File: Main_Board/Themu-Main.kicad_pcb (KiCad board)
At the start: 2 copper layers, 20.1 x 56.6 mm, 49 parts, among them J1 USB_B_Micro, J2 Conn_01x02, J3 Conn_01x08, Q1 mmbt2222, Q2 mmbt2222, Q3 DMP2045U, U1 CP2104, U2 AP2112K-3.3, U3 ESP32-WROOM-32, U4 MCP73831-2-OT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

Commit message: Added adapter board for 5 flex sensors and 1 button
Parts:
- L1: footprint Themu_FP_Lib:LED APTF1616LSEEZGKQBKC -> Main_Board:LED_APTF1616LSEEZGKQBKC
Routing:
- net GND: vias 17 -> 12
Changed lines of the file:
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@@
     (thickness 1.6)
     (drawings 4)
-    (tracks 898)
+    (tracks 894)
     (zones 0)
     (modules 49)
@@
     (add_net VBUS)
   )
+  (module Main_Board:LED_APTF1616LSEEZGKQBKC (layer F.Cu)
+    (at 111.506 75.946 270)
+    (fp_text reference L1 (at 0 2.032 90) (layer F.SilkS)
+      (effects (font (size 1 1) (thickness 0.15)))
+    )
+    (fp_text value LED_ARGB (at 0 -1.905 90) (layer F.Fab)
+      (effects (font (size 1 1) (thickness 0.15)))
+    )
+    (fp_line (start -0.127 -0.8) (end 0.127 -0.8) (layer F.SilkS) (width 0.12))
+    (fp_line (start -0.127 0.8) (end 0.127 0.8) (layer F.SilkS) (width 0.12))
+    (fp_line (start -1.524 -1.016) (end 1.524 -1.016) (layer F.CrtYd) (width 0.05))
+    (fp_line (start 1.524 -1.016) (end 1.524 1.016) (layer F.CrtYd) (width 0.05))
+    (fp_line (start 1.524 1.016) (end -1.524 1.016) (layer F.CrtYd) (width 0.05))
+    (fp_line (start -1.524 1.016) (end -1.524 -1.016) (layer F.CrtYd) (width 0.05))
+    (fp_line (start 0.127 0.254) (end 0.127 0.8) (layer F.SilkS) (width 0.12))
+    (pad 4 smd rect (at 0.875 -0.5 270) (size 0.85 0.5) (layers F.Cu F.Paste F.Mask)
+      (net 37 "Net-(L1-Pad4)"))
+    (pad 1 smd rect (at 0.875 0.5 270) (size 0.85 0.5) (layers F.Cu F.Paste F.Mask)
+      (net 2 +3V3))
+    (pad 2 smd rect (at -0.875 0.5 270) (size 0.85 0.5) (layers F.Cu F.Paste F.Mask)
+      (net 32 "Net-(L1-Pad2)"))
+    (pad 3 smd rect (at -0.875 -0.5 270) (size 0.85 0.5) (layers F.Cu F.Paste F.Mask)
+      (net 31 "Net-(L1-Pad3)"))
+    (model "C:/Users/germi/Downloads/User Library-LED_0605/User Library-LED_0605.STEP"
+      (at (xyz 0 0 0))
+      (scale (xyz 1 1 1))
+      (rotate (xyz 0 0 0))
+    )
+  )
   (module RF_Module:ESP32-WROOM-32 (layer F.Cu)
     (at 103.124 56.007)
@@
     )
   )
-  (module "Themu_FP_Lib:LED APTF1616LSEEZGKQBKC" (layer F.Cu)
-    (at 111.506 75.946 270)
-    (fp_text reference L1 (at -2.286 -0.635 90) (layer F.SilkS)
-      (effects (font (size 0.7 0.7) (thickness 0.1524)))
-    )
-    (fp_text value LED_ARGB (at 0 -1.905 90) (layer F.Fab)
-      (effects (font (size 1 1) (thickness 0.15)))
-    )
-    (fp_line (start -0.127 -0.8) (end 0.127 -0.8) (layer F.SilkS) (width 0.12))
-    (fp_line (start -0.127 0.8) (end 0.127 0.8) (layer F.SilkS) (width 0.12))
-    (fp_line (start -1.524 -1.016) (end 1.524 -1.016) (layer F.CrtYd) (width 0.05))
-    (fp_line (start 1.524 -1.016) (end 1.524 1.016) (layer F.CrtYd) (width 0.05))
-    (fp_line (start 1.524 1.016) (end -1.524 1.016) (layer F.CrtYd) (width 0.05))
-    (fp_line (start -1.524 1.016) (end -1.524 -1.016) (layer F.CrtYd) (width 0.05))
-    (fp_line (start 0.127 0.254) (end 0.127 0.8) (layer F.SilkS) (width 0.12))
-    (pad 4 smd rect (at 0.875 -0.5 270) (size 0.85 0.5) (layers F.Cu F.Paste F.Mask)
-      (net 37 "Net-(L1-Pad4)"))
-    (pad 1 smd rect (at 0.875 0.5 270) (size 0.85 0.5) (layers F.Cu F.Paste F.Mask)
-      (net 2 +3V3))
-    (pad 2 smd rect (at -0.875 0.5 270) (size 0.85 0.5) (layers F.Cu F.Paste F.Mask)
-      (net 32 "Net-(L1-Pad2)"))
-    (pad 3 smd rect (at -0.875 -0.5 270) (size 0.85 0.5) (layers F.Cu F.Paste F.Mask)
-      (net 31 "Net-(L1-Pad3)"))
-    (model "C:/Users/germi/Downloads/User Library-LED_0605/User Library-LED_0605.STEP"
-      (at (xyz 0 0 0))
-      (scale (xyz 1 1 1))
-      (rotate (xyz 0 0 0))
-    )
-  )
   (module Connector_JST:JST_PH_S2B-PH-K_1x02_P2.00mm_Horizontal (layer F.Cu)
     (at 101.727 91.694 270)
@@
     (tags "capacitor handsolder")
     (attr smd)
-    (fp_text reference C10 (at 0.127 -4.826 90) (layer B.SilkS)
+    (fp_text reference C10 (at -0.889 -8.001 90) (layer B.SilkS)
       (effects (font (size 0.7 0.7) (thickness 0.1524)) (justify mirror))
     )
@@
     (tags "capacitor handsolder")
     (attr smd)
-    (fp_text reference C11 (at 0.127 -5.334 90) (layer B.SilkS)
+    (fp_text reference C11 (at -0.127 -8.382 90) (layer B.SilkS)
       (effects (font (size 0.7 0.7) (thickness 0.1524)) (justify mirror))
     )
@@
     (tags "resistor handsolder")
     (attr smd)
-    (fp_text reference R13 (at 0.127 -4.318 90) (layer B.SilkS)
+    (fp_text reference R13 (at -1.778 -7.493 90) (layer B.SilkS)
       (effects (font (size 0.7 0.7) (thickness 0.1524)) (justify mirror))
     )
@@
   (gr_line (start 113.157 96.393) (end 93.091 96.393) (layer Edge.Cuts) (width 0.1))
   (via (at 100.457 56.896) (size 0.8) (drill 0.4) (layers F.Cu B.Cu) (net 1))
-  (via (at 102.235 53.213) (size 0.8) (drill 0.4) (layers F.Cu B.Cu) (net 1))
-  (via (at 102.997 56.134) (size 0.8) (drill 0.4) (layers F.Cu B.Cu) (net 1))
-  (via (at 101.346 56.134) (size 0.8) (drill 0.4) (layers F.Cu B.Cu) (net 1))
-  (via (at 103.759 56.896) (size 0.8) (drill 0.4) (layers F.Cu B.Cu) (net 1))
   (via (at 107.315 71.882) (size 0.8) (drill 0.4) (layers F.Cu B.Cu) (net 1))
   (segment (start 109.728 75.071) (end 109.728 74.168) (width 0.1524) (layer F.Cu) (net 1))
@@
   (segment (start 94.615 46.609) (end 111.633 46.609) (width 0.1524) (layer F.Cu) (net 1))
   (segment (start 102.124 56.88) (end 102.124 55.252) (width 0.1524) (layer F.Cu) (net 1))
-  (via (at 102.124 56.88) (size 0.8) (drill 0.4) (layers F.Cu B.Cu) (net 1))
   (segment (start 109.855 49.911) (end 108.712 51.054) (width 0.1524) (layer B.Cu) (net 1))
   (segment (start 102.124 55.252) (end 102.124 55.252) (width 0.1524) (layer F.Cu) (net 1))
   (segment (start 102.183 55.193) (end 102.124 55.252) (width 0.1524) (layer F.Cu) (net 1))
-  (via (at 102.183 55.193) (size 0.8) (drill 0.4) (layers F.Cu B.Cu) (net 1))
   (segment (start 109.22 79.756) (end 109.728 79.248) (width 0.1524) (layer F.Cu) (net 1))
   (segment (start 109.728 79.248) (end 110.998 79.248) (width 0.1524) (layer F.Cu) (net 1))
@@
   (segment (start 102.235 60.452) (end 102.235 59.055) (width 0.1524) (layer F.Cu) (net 1))
   (segment (start 102.235 59.055) (end 102.124 58.944) (width 0.1524) (layer F.Cu) (net 1))
+  (segment (start 102.124 55.252) (end 102.124 55.252) (width 0.1524) (layer F.Cu) (net 1))
+  (via (at 102.124 55.252) (size 3) (drill 2.8) (layers F.Cu B.Cu) (net 1) (status 1000000))
   (segment (start 101.854 78.867) (end 101.8215 78.8345) (width 0.1524) (layer F.Cu) (net 2))
   (segment (start 108.27 80.434) (end 108.27 78.801) (width 0.1524) (layer F.Cu) (net 2))
@@
     (connect_pads (clearance 0.3048))
     (min_thickness 0.1524)
-    (fill yes (arc_segments 32) (thermal_gap 0.254) (thermal_bridge_width 0.2032))
+    (fill yes (arc_segments 32) (thermal_gap 0.254) (thermal_bridge_width 0.3))
     (polygon
       (pts
@@
     (connect_pads (clearance 0.3048))
     (min_thickness 0.1524)
-    (fill yes (arc_segments 32) (thermal_gap 0.254) (thermal_bridge_width 0.2032))
+    (fill yes (arc_segments 32) (thermal_gap 0.254) (thermal_bridge_width 0.3))
     (polygon
       (pts

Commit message: Partial commit
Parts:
- added R22: 1K, Resistor_SMD:R_0603_1608Metric_Pad1.05x0.95mm_HandSolder, F.Cu at (118.4, 77.7)
- R15, R16, R17, R18, R19: value 1K -> 47K
- moved J3 51.6 mm to (132.6, 52.3), turned to 90 degrees
- moved R11 35.7 mm to (132.0, 58.7), turned to 180 degrees
- moved C9 34.7 mm to (132.0, 60.2), turned to 0 degrees
- moved R19 33.9 mm to (132.0, 61.7), turned to 180 degrees
- moved R18 33.1 mm to (132.0, 63.2), turned to 180 degrees
- moved R17 32.5 mm to (132.0, 64.8), turned to 180 degrees
- moved R16 32.0 mm to (132.0, 66.3), turned to 180 degrees
- moved J1 31.9 mm to (87.2, 69.0), turned to 270 degrees
- moved J2 31.9 mm to (88.6, 62.6), turned to 180 degrees
- moved R15 31.7 mm to (132.0, 67.8), turned to 180 degrees
- moved R5 31.5 mm to (132.0, 69.3), turned to 0 degrees
- moved C8 28.7 mm to (92.7, 59.6), turned to 90 degrees
- moved R4 26.0 mm to (95.1, 59.4), turned to 90 degrees
- moved Q3 24.7 mm to (93.5, 64.1), turned to 90 degrees
- moved D2 23.4 mm to (93.5, 67.4), turned to 180 degrees
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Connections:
- J3 pad 7: /ESP32-WROOM-32/BTN -> /Peripherials/BUTTON
- J3 pad 8: +3V3 -> (no net)
- R15 pad 1: GND -> +3V3
- R16 pad 1: GND -> +3V3
- R17 pad 1: GND -> +3V3
- R18 pad 1: GND -> +3V3
- R19 pad 1: GND -> +3V3
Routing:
- net +3V3: track 112.6 -> 94.1 mm
- net GND: track 252.9 -> 248.9 mm
- net /ESP32-WROOM-32/BTN: track 29.7 -> 27.9 mm
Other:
- board size 20.1 x 56.6 mm -> 56.6 x 23.2 mm

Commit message: Rev 2.0 commit. INTI revision.
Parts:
- removed L1: LED_ARGB, Main_Board:LED_APTF1616LSEEZGKQBKC
- added D3: LED_ARGB, Main_Board:LED_APTF1616LSEEZGKQBKC, F.Cu at (64.5, 88.9)
- C5, C6, C7, R10, R22: moved to B.Cu
- moved C9 65.1 mm to (71.5, 84.5), turned to 90 degrees
- moved R11 64.0 mm to (73.4, 84.5), turned to 270 degrees
- moved C14 63.9 mm to (53.1, 100.3), turned to 180 degrees
- moved R19 61.0 mm to (75.3, 84.5), turned to 270 degrees
- moved C1 60.5 mm to (53.1, 97.8), turned to 180 degrees
- moved R18 58.7 mm to (77.2, 84.5), turned to 270 degrees
- moved R17 56.4 mm to (79.1, 84.5), turned to 270 degrees
- moved C13 56.4 mm to (67.7, 95.9), turned to 90 degrees
- moved U3 54.3 mm to (77.9, 92.1)
- moved R16 54.1 mm to (81.0, 84.5), turned to 270 degrees
- moved J3 53.9 mm to (86.7, 80.6)
- moved Q2 53.8 mm to (64.5, 99.7)
- moved R1 53.5 mm to (65.4, 95.9)
- moved R2 53.5 mm to (63.9, 95.9)
- moved Q1 53.5 mm to (64.5, 92.1)
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- renumbered L2 to D1
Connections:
- J3 pad 1: GND -> (no net)
- J3 pad 8: (no net) -> GND
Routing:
- net GND: track 248.9 -> 103.0 mm
- net /ESP32-WROOM-32/FLX1: track 48.9 -> 10.6 mm
- net /ESP32-WROOM-32/FLX2: track 45.3 -> 8.70 mm
- net /ESP32-WROOM-32/FLX3: track 40.2 -> 7.91 mm
- net /ESP32-WROOM-32/FLX4: track 36.7 -> 7.64 mm
- net /ESP32-WROOM-32/FLX5: track 33.8 -> 8.43 mm
- net +3V3: track 94.1 -> 117.7 mm, vias 6 -> 7
- net /ESP32-WROOM-32/ADC1_CH0: track 55.4 -> 40.8 mm, vias 2 -> 4
- net /ESP32-WROOM-32/BTN: track 27.9 -> 13.4 mm
- net VBUS: track 29.4 -> 42.2 mm, vias 0 -> 3
- net /ESP32-WROOM-32/IO26: track 19.0 -> 6.25 mm
- net /ESP32-WROOM-32/IO27: track 17.3 -> 5.98 mm
- net /ESP32-WROOM-32/RTS: track 18.0 -> 7.07 mm, vias 2 -> 0
- net /ESP32-WROOM-32/IO12: track 16.9 -> 6.35 mm
- net /Peripherials/AD0: track 2.95 -> 13.4 mm
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- removed copper zone on F.Cu, net +BATT
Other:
- board size 56.6 x 23.2 mm -> 49.5 x 23.5 mm
- net class BATT removed
- net class Net-(C2-Pad1) removed
- net class VBUS removed
- board text added: "*Placement grid: 25 mils (0.635 mm) (60 mils between R1 and R2) *Routing grid: 2.5 mils (0.0635 mm) *Tracks width: 6 mils (0.1524 mm) *Clearance: 8 mils (0.2032 mm) *Vias drill/size: 15.748/31.496 mils (0.4/0.8 mm) *Surface Finish: HASL Lead Free. *Copper-to-edge distance: 20 mils (0.51 mm) *Board size: 1950x925 mils (49.5/23.5 mm)"
- board text added: "+"
- board text added: "B1"
- board text added: "F1"
- board text added: "F2"
- board text added: "F3"
- board text added: "F4"
- board text added: "F5"
- board text added: "GND"
- board text added: "NC"
- board text added: "Rev: 02 IND. ARG."
- board text added: "Themu"

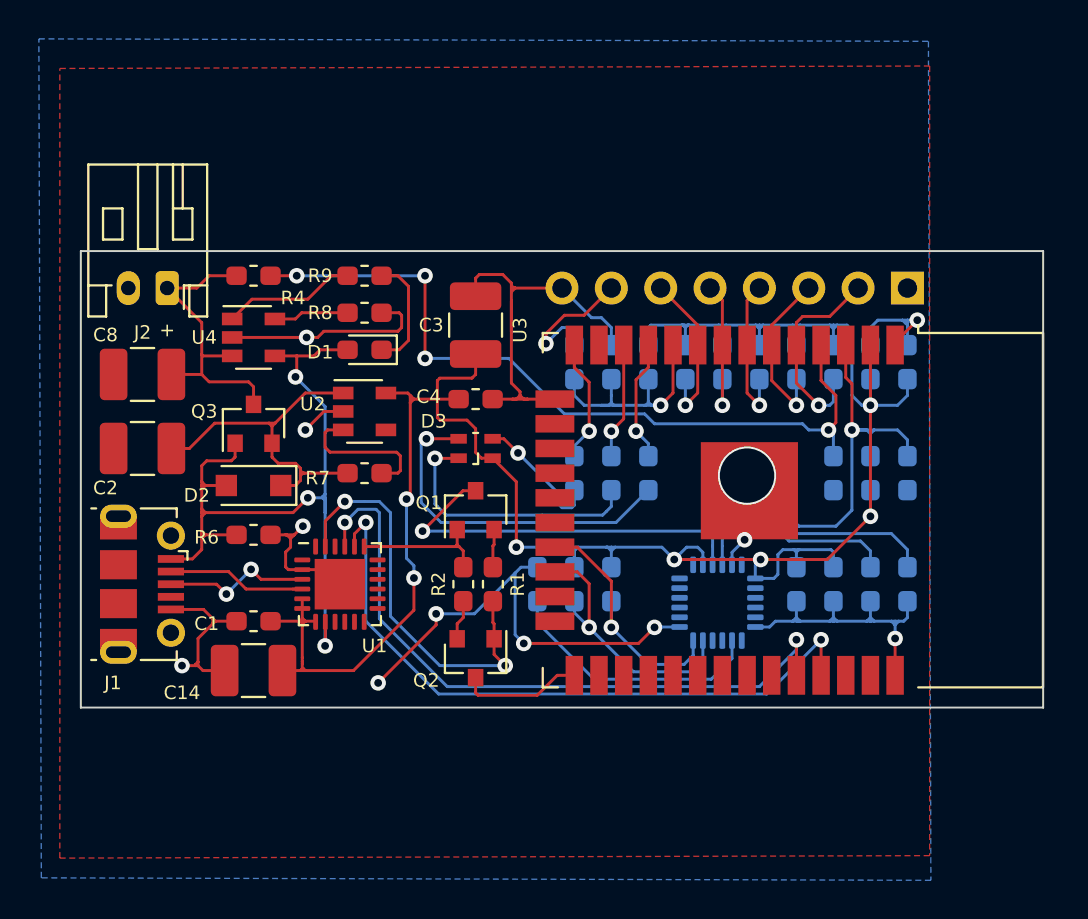
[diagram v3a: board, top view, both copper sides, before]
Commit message: Resolving issues. (#9)
- Bottom silk legend changed.
- New tracing rules added for power supply lines.
- D3 led changed for QBLP655R-RGB. 3D model missing.
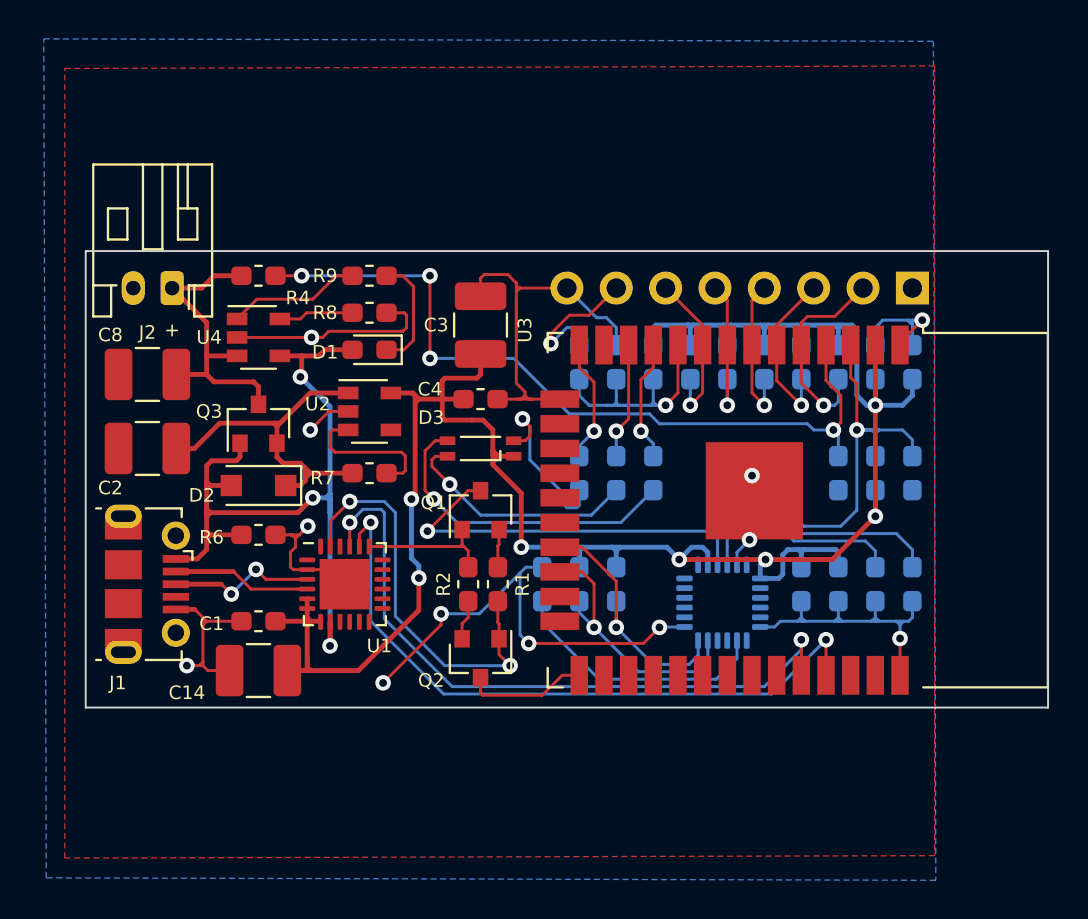
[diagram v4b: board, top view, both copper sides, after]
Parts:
- C1, C10, C11, C5, C6: value 0.1uF 25V X7R -> 0.1uF 100V X7R
- C13: value 2200pF 50V X7R -> 0.0022uF 200V X7R
- C14, C2, C3, C8: value 10uF 25V X7R -> 10uF 6.3V X5R
- C4: value 1uF 25V X5R -> 1uF 6.3V X5R
- C9: value 1000pF 25V X5R -> 0.1uF 100V X7R
- D3: value LED_ARGB -> LED_RABG; footprint Main_Board:LED_APTF1616LSEEZGKQBKC -> Main_Board:LED_QBLP655R_RGB
- Q3: value DMP2045U -> DMG2305U
- R20: value 1K -> 374R
- R21: value 1K -> 232R
- R3: value 1K -> 560R
- moved C1 0.25 mm to (53.3, 97.8)
- moved C10 0.25 mm to (85.1, 95.9)
- moved C11 0.25 mm to (83.2, 95.9)
- moved C12 0.25 mm to (81.3, 95.9)
- moved C14 0.25 mm to (53.3, 100.3)
- moved C5 0.25 mm to (87.0, 90.2)
- moved C6 0.25 mm to (85.1, 84.5)
- moved C7 0.25 mm to (87.0, 84.5)
- moved D2 0.25 mm to (53.3, 90.8)
- moved J2 0.25 mm to (48.9, 80.6)
- moved J3 0.25 mm to (87.0, 80.6)
- moved Q3 0.25 mm to (53.3, 87.6)
- moved R1 0.25 mm to (65.7, 95.9)
- moved R10 0.25 mm to (85.1, 90.2)
- moved R13 0.25 mm to (87.0, 95.9)
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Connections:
- net Net-(C2-Pad1) renamed /Power/RegIn
- D3 pad 1: +3V3 -> Net-(D3-Pad1)
- D3 pad 2: Net-(D3-Pad2) -> +3V3
- R20 pad 2: Net-(D3-Pad3) -> Net-(D3-Pad4)
- R21 pad 2: Net-(D3-Pad2) -> Net-(D3-Pad1)
- R3 pad 2: Net-(D3-Pad4) -> Net-(D3-Pad3)
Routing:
- net Net-(D3-Pad2): track 13.9 -> 0.00 mm, vias 1 -> 0
- net Net-(D3-Pad1): track 0.00 -> 12.3 mm, vias 0 -> 1
- net Net-(D3-Pad4): track 6.83 -> 16.5 mm
- net Net-(D3-Pad3): track 17.9 -> 8.97 mm
- net +3V3: track 117.7 -> 119.5 mm
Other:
- net class PowerLines added: clearance 0.2032, trace_width 0.25, via_dia 0.8, via_drill 0.4
- board text added: "Rev: 03 Diseño Argentino"
- board text removed: "Rev: 02 IND. ARG."
